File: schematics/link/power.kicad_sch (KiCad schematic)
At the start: 36 parts, among them J5 12V Alt Supply, U1 LM27762, U2 Ag9912-LP, U3 TC1262-33

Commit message: update(pcb): combining modules
Want to try a different layout, but like where I am at right now
Planning to branch off of this one and see where it goes
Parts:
- C5: footprint Capacitor_SMD:C_0805_2012Metric -> Capacitor_SMD:C_0603_1608Metric
- U2: symbol Link_Components:Ag9912-MTB -> Link_Components:Ag9912-LP; now in the parts list
- renumbered D11 to D12, D12 to D13, D13 to D16, J5 to J2
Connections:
- net at JP6.3 (B), TP6.1: now also U2.3 (-VDC); no longer U2.1 (+VDC)
- net GND renamed +VDC
- net +VDC: now also U2.1 (+VDC)
- net V+ renamed VIN+
- net VIN+: now also U2.5 (VIN+), U2.6 (VIN+); no longer U2.4 (VIN+)
- net V- renamed VIN-
- net VIN-: now also U2.7 (VIN-), U2.8 (VIN-); no longer U2.5 (VIN-)
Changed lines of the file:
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@@
 		)
 	)
-	(hierarchical_label "V-"
+	(hierarchical_label "Vin-"
 		(shape input)
 		(at 180.34 41.91 180)
@@
 		)
 	)
-	(hierarchical_label "V+"
+	(hierarchical_label "Vin+"
 		(shape input)
 		(at 180.34 34.29 180)
@@
 		(dnp no)
 		(fields_autoplaced yes)
-		(property "Reference" "D13"
+		(property "Reference" "D16"
 			(at 232.41 64.7699 90)
 			(show_name no)
@@
 			(project "link"
 				(path "/e6a73b1b-9233-47b9-8d6b-253608bed688/dab49fcf-3c96-4274-9192-150c01f7c53c"
-					(reference "D13")
+					(reference "D16")
 					(unit 1)
 				)
@@
 		(in_pos_files yes)
 		(dnp no)
-		(property "Reference" "D12"
+		(property "Reference" "D13"
 			(at 192.278 37.084 90)
 			(show_name no)
@@
 			(project "link"
 				(path "/e6a73b1b-9233-47b9-8d6b-253608bed688/dab49fcf-3c96-4274-9192-150c01f7c53c"
-					(reference "D12")
+					(reference "D13")
 					(unit 1)
 				)
@@
 		(dnp no)
 		(fields_autoplaced yes)
-		(property "Reference" "D11"
+		(property "Reference" "D12"
 			(at 76.2 46.0374 90)
 			(show_name no)
@@
 			(project "link"
 				(path "/e6a73b1b-9233-47b9-8d6b-253608bed688/dab49fcf-3c96-4274-9192-150c01f7c53c"
-					(reference "D11")
+					(reference "D12")
 					(unit 1)
 				)
@@
 			)
 		)
-		(property "Footprint" "Capacitor_SMD:C_0805_2012Metric"
+		(property "Footprint" "Capacitor_SMD:C_0603_1608Metric"
 			(at 82.55 54.61 0)
 			(hide yes)
@@
 	)
 	(symbol
-		(lib_id "Link_Components:Ag9912-MTB")
+		(lib_id "Link_Components:Ag9912-LP")
 		(at 213.36 38.1 0)
 		(unit 1)
 		(body_style 1)
 		(exclude_from_sim no)
-		(in_bom no)
+		(in_bom yes)
 		(on_board yes)
 		(in_pos_files yes)
@@
 		(pin "4"
 		)
+		(pin "6"
+		)
+		(pin "7"
+		)
+		(pin "8"
+		)
 		(instances
 			(project "link"
@@
 		(in_pos_files yes)
 		(dnp no)
-		(property "Reference" "J5"
+		(property "Reference" "J2"
 			(at 205.74 67.3101 0)
 			(show_name no)
@@
 			(project "link"
 				(path "/e6a73b1b-9233-47b9-8d6b-253608bed688/dab49fcf-3c96-4274-9192-150c01f7c53c"
-					(reference "J5")
+					(reference "J2")
 					(unit 1)
 				)

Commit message: update(link): finalized placements
Still some work to be done:
1. Fix planes under RJ45 connector, probably should keep out if possible
2. Fix silkscreening
3. Fix isolated filled zones
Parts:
- removed D12: PGOOD, Diode_SMD:D_0603_1608Metric, symbol Device:LED
- removed R5: 1k, Resistor_SMD:R_0402_1005Metric, symbol Device:R_Small_US
- removed TP4: Vin+, Link_Footprints:TestPoint_Pad_D1.5mm, symbol Connector:TestPoint
- removed TP6: Vout+, Link_Footprints:TestPoint_Pad_D1.5mm, symbol Connector:TestPoint
- C11: renamed from C6; footprint Capacitor_SMD:C_0603_1608Metric -> Capacitor_SMD:C_0402_1005Metric
- C6: renamed from C4; footprint Capacitor_SMD:C_0603_1608Metric -> Capacitor_SMD:C_0402_1005Metric
- U2: renamed from U1; footprint Package_SON:WSON-12-1EP_3x2mm_P0.5mm_EP1x2.65_ThermalVias -> Link_Footprints:LM27762
- renumbered C5 to C10, C8 to C12, C10 to C13, C9 to C14, C11 to C15, C12 to C16, C13 to C8, C14 to C9, D13 to D8, D16 to D9, J2 to J5, JP6 to JP3, JP5 to JP4, R8 to R6, R9 to R7, R6 to R8, R7 to R9, TP1 to TP3, TP5 to TP4, TP9 to TP5, TP3 to TP6, TP2 to TP7, TP7 to TP9, U2 to U1
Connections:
- net +VDC: now also JP3.3 (B); no longer C11.2, C12.2, C13.2, C14.2, C15.2, C16.2, C6.2, C7.2, C8.2, C9.2, D9.2 (A), J5.1 (Pin_1), PS1.2 (GND), R7.2, R9.1, TP7.1, U2.13 (PAD), U2.4 (GND), U3.2 (GND)
- net GND: now reaches U1.3 (-VDC)
- net GND: now also C11.2, C12.2, C13.2, C14.2, C15.2, C16.2, C6.2, C7.2, C8.2, C9.2, D9.2 (A), J5.1 (Pin_1), PS1.2 (GND), R7.2, R9.1, TP7.1, U2.1 (PGOOD), U2.13 (PAD), U2.4 (GND), U3.2 (GND); no longer JP3.3 (B)

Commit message: update(link): GPT review
GPT suggested a few changes:
1. ADS131M02 RC input network (not added)
   this maybe should be added as DNP, but AFE already
   handles basic filtering

2. Reroute S2+ on top plane (added)
3. Ag9912 minumum load (added)
   The minimum load requirement is 100mA at 12V,
   I added an LED for a baseline minimum, but
   digital ICs should get to 100mA alone
4. Remove input select jumper for production (not added)
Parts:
- added D11: +12V, Diode_SMD:D_0603_1608Metric, symbol Device:LED
- added R42: 220, Resistor_SMD:R_0603_1608Metric, symbol Device:R_Small_US
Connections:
- net +12V: now also R42.1
- net GND: now also D11.1 (K)
- new net: D11.2 (A), R42.2

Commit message: fix: git history
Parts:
- removed F1: Fuse, Link_Footprints:0154Series_LTF, symbol Device:Fuse
- added F2: Fuse, Link_Footprints:0154Series_LTF, symbol Device:Fuse
- added TP18: Vin+, Link_Footprints:TestPoint_Pad_D1.5mm, symbol Connector:TestPoint
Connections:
- net +12V: now also D9.1 (K), F2.2; no longer JP3.2 (C)
- net VIN+: now also TP18.1
- net at JP3.1 (A): now also J5.2 (Pin_2); no longer D9.1 (K)
- new net: F2.1, JP3.2 (C)
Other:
- moved on the sheet: C8, C9, D8, D9, J5, JP3, TP4, TP5, U1

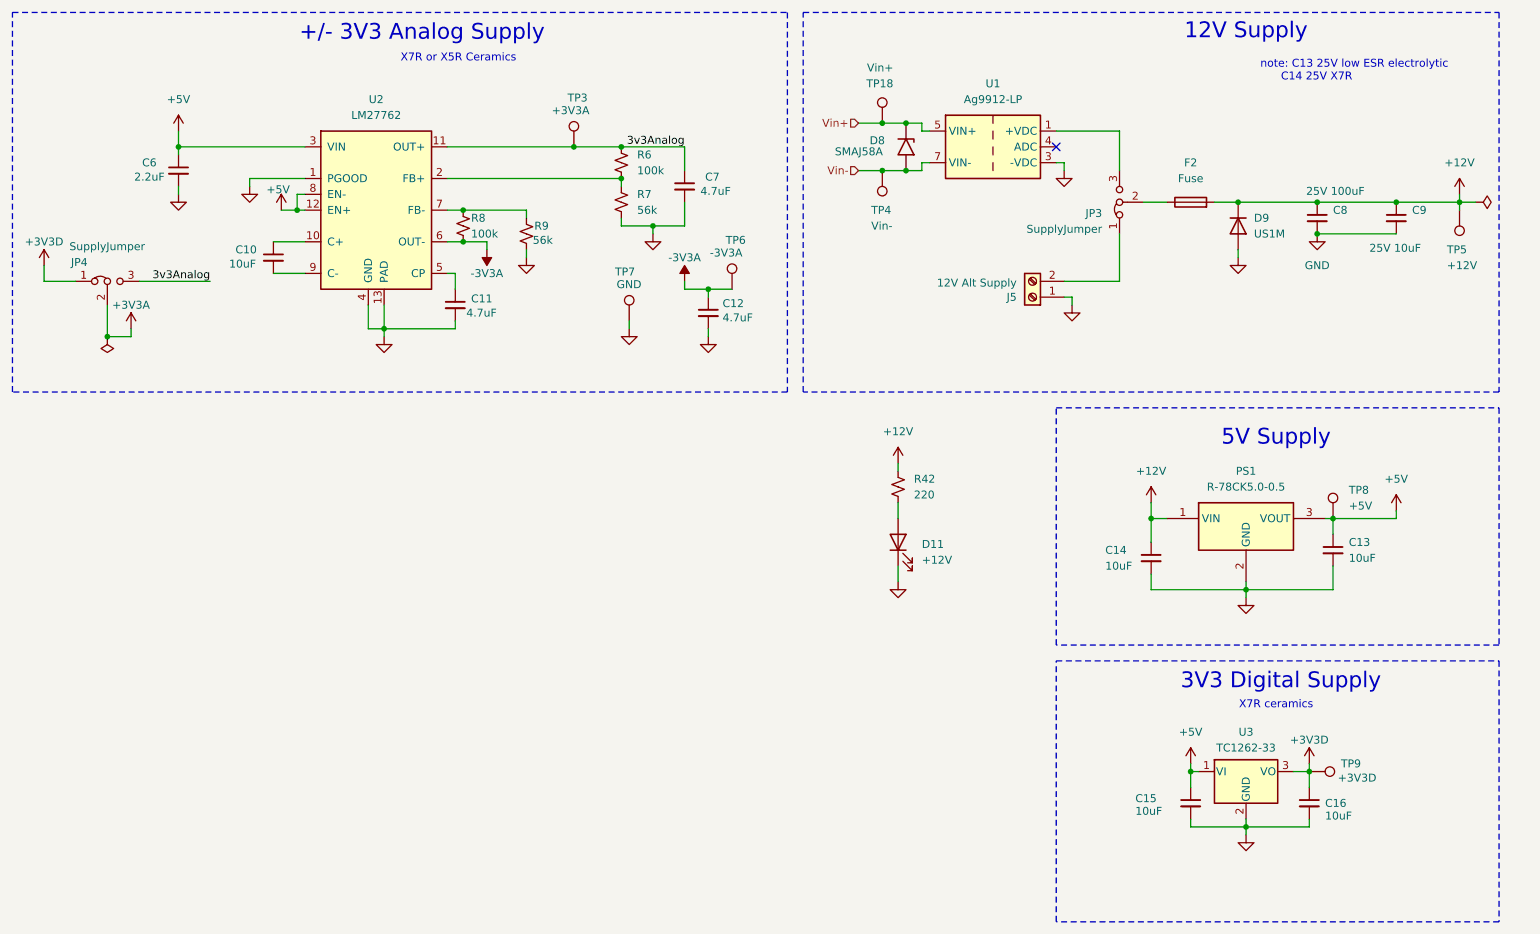
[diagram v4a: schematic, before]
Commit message: update(review):
1. Take gain resistor out of AFE filter
2. Breakout I2C
3. Move fuse to cover both 12V rails
4. Silkscreens
5. More testpoints + change to clip ons
6. Match ADC input max and filter output max
7. Add shunt for current resistors
8. Thermocouples
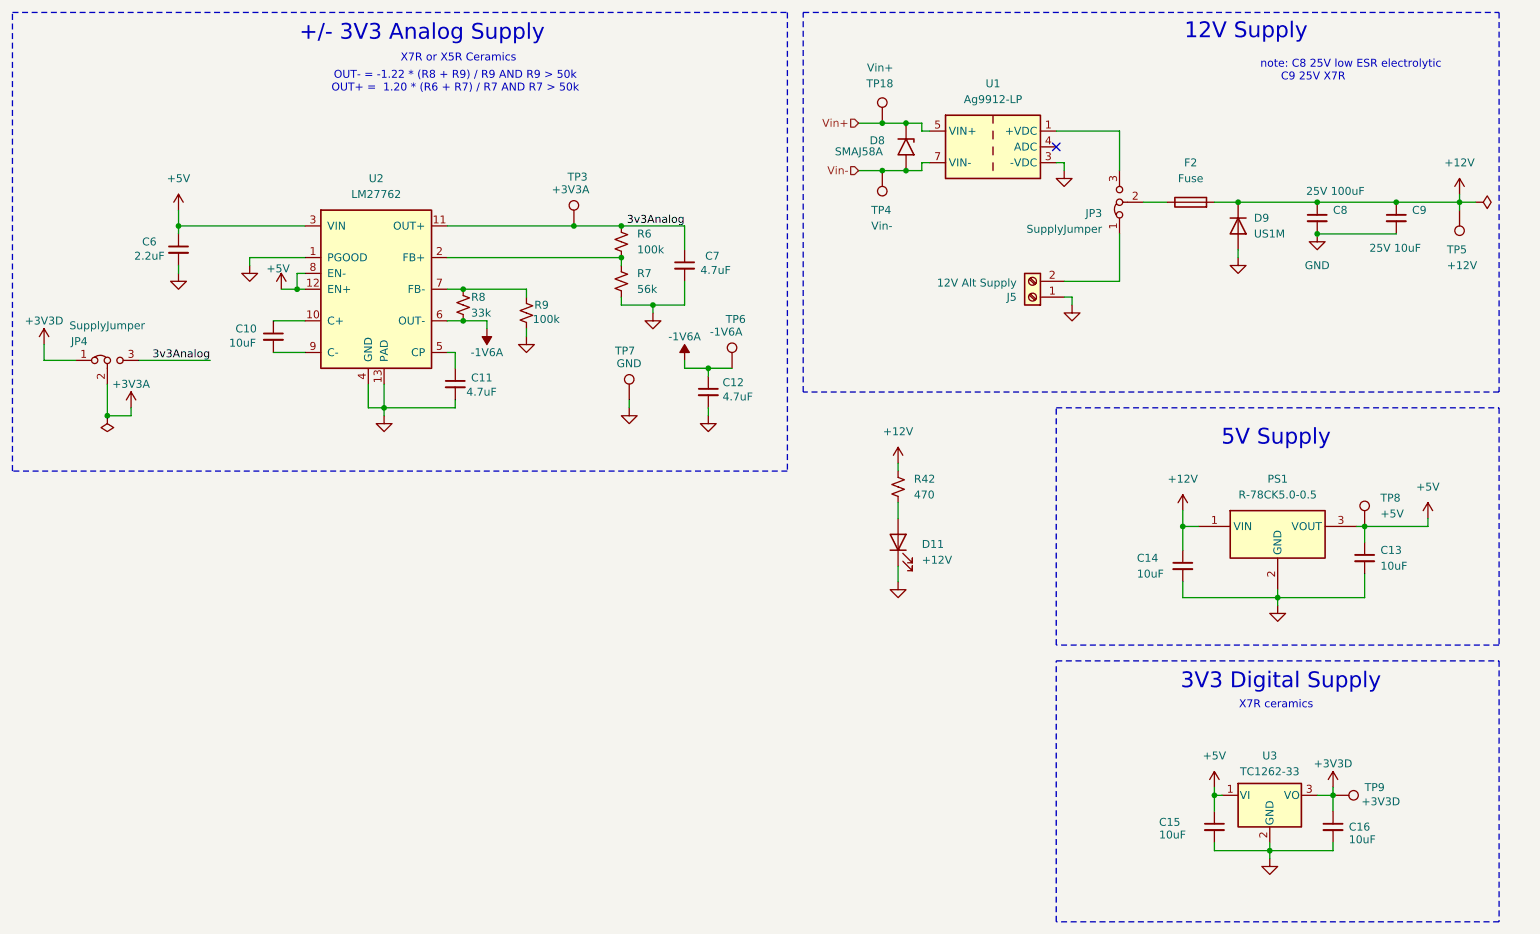
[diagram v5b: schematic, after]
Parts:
- C10, C13, C14, C15, C16: footprint Capacitor_SMD:C_0603_1608Metric -> Capacitor_SMD:C_0805_2012Metric; MPN (none) -> GCM21BR71A106KE22L
- C11: MPN (none) -> GRM155R60G475ME47J
- C12, C7: MPN (none) -> GRM188Z71C475KE21D
- C6: footprint Capacitor_SMD:C_0402_1005Metric -> Capacitor_SMD:C_0603_1608Metric; MPN (none) -> GRM188R71A225KE15D
- C8: footprint Capacitor_THT:CP_Radial_D6.3mm_P2.50mm -> Capacitor_SMD:CP_Elec_6.3x7.7; MPN (none) -> UUD1E101MCL1GS
- C9: MPN (none) -> GRM31CR71E106KA12L
- D11: MPN (none) -> 150060BS75020
- D8: MPN (none) -> SMAJ58A
- D9: MPN (none) -> US1M
- F2: MPN (none) -> 0154.750DR
- J5: MPN (none) -> 1711725
- JP3, JP4: MPN (none) -> 61300311121
- PS1: MPN (none) -> R-78CK5.0-0.5
- R42: value 220 -> 470; MPN (none) -> RC0603FR-07470RL
- R6: MPN (none) -> RT0402BRD07100KL
- R7: MPN (none) -> RT0402BRD0756KL
- R8: value 100k -> 33k; MPN (none) -> RT0402BRD0733KL
- R9: value 56k -> 100k; MPN (none) -> RT0402BRD07100KL
- TP18, TP3, TP4, TP5, TP8, TP9: MPN (none) -> N/A
- TP6: value -3V3A -> -1V6A; MPN (none) -> N/A
- TP7: footprint Link_Footprints:TestPoint_Pad_D1.5mm -> Link_Footprints:Keystone1573-2; MPN (none) -> 1573-2; now in the parts list
- U1: footprint Converter_DCDC:Converter_DCDC_Silvertel_Ag99xxLP_THT -> Link_Footprints:Silvertel_Ag99xxLP; MPN (none) -> AG9912LP
- U2: MPN (none) -> LM27762DSSR
- U3: MPN (none) -> TC1262-3.3VDBTR
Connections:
- net -3V3A renamed -1V6A
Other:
- note added: "OUT- = -1.22 * (R8 + R9) / R9 AND R9 > 50k OUT+ = 1.20 * (R6 + R7) / R7 AND R7 > 50k"
- note added: "note: C8 25V low ESR electrolytic C9 25V X7R"
- note removed: "note: C13 25V low ESR electrolytic C14 25V X7R"
- moved on the sheet: C10, C11, C12, C13, C14, C15, C16, C6, C7, JP4, PS1, R6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

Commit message: GPT review
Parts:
- removed U3: TC1262-33, Link_Footprints:TC1262, symbol Regulator_Linear:TC1262-33
- added U10: AP2112K-3.3, Package_TO_SOT_SMD:SOT-23-5, symbol Regulator_Linear:AP2112K-3.3
- C10, C13, C14: LCSC C326595 -> (none); MPN GCM21BR71A106KE22L -> GRM21BR61E106MA73L
- C11: footprint Capacitor_SMD:C_0402_1005Metric -> Capacitor_SMD:C_0603_1608Metric; LCSC C49326649 -> (none); MPN GRM155R60G475ME47J -> GRM188Z71C475KE21D
- C12, C7: LCSC C49326649 -> (none)
- C15, C16: value 10uF -> 1uF; footprint Capacitor_SMD:C_0805_2012Metric -> Capacitor_SMD:C_0603_1608Metric; LCSC C326595 -> (none); MPN GCM21BR71A106KE22L -> GCM188R71C105KA64D
- C6: LCSC C43922 -> (none)
- C8: LCSC C165558 -> (none)
- C9: LCSC C70462 -> (none)
- D8: LCSC C5121740 -> (none)
- D9: LCSC C412437 -> (none)
- F2: LCSC C206917 -> (none)
- J5: LCSC C89120 -> (none)
- PS1: LCSC C28216137 -> (none); Manufacturer_Part_Number R-78CK3.3-0.5 -> (none)
- R42: value 470 -> 2.2k; MPN RC0603FR-07470RL -> (none)
- R6, R8: LCSC C25741 -> (none)
- R7, R9: LCSC C103107 -> (none)
- U2: LCSC C473398 -> (none)
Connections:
- net +3V3D: now also U10.5 (VOUT)
- net +5V: now also U10.1 (VIN), U10.3 (EN)
- net GND: now also U10.2 (GND)
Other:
- moved on the sheet: TP9

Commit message: GPT review pt2
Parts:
- D11: mpn 598-8E90-107F -> (none)
- R42: MPN (none) -> RC0603JR-072K2L
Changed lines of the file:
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@@
 			)
 		)
-		(property "MPN" ""
+		(property "MPN" "RC0603JR-072K2L"
 			(at 182.88 91.44 0)
 			(hide yes)
@@
 			(hide yes)
 			(show_name no)
-			(do_not_autoplace no)
-			(effects
-				(font
-					(size 1.27 1.27)
-				)
-			)
-		)
-		(property "mpn" " 598-8E90-107F "
-			(at 182.88 100.33 90)
-			(hide yes)
-			(show_name no)
